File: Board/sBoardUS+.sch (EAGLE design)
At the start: 40 parts, among them IC1 PIC18F2580-E/SO, IC2 74AC32D, IC3 MAX481CSA, IC4 MC1525TT

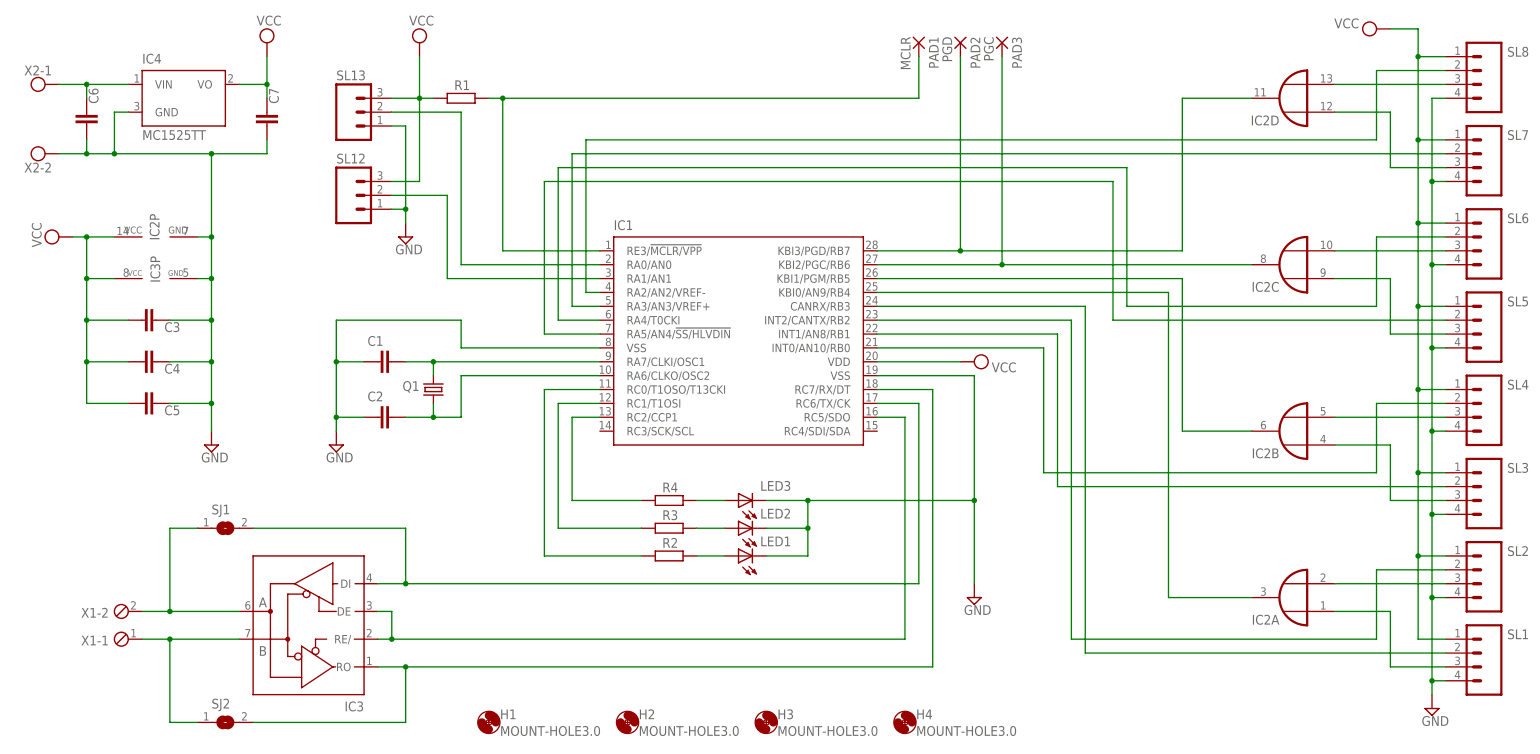
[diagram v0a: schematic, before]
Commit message: Aggiornamento struttura e modifiche
Cambiata la cartella di lavoro e ricreato il file BRD, modificato lo
schema aggiungendo il led di TX/RX, aggiunto il connettore I2C, cambiato
il quarzo.
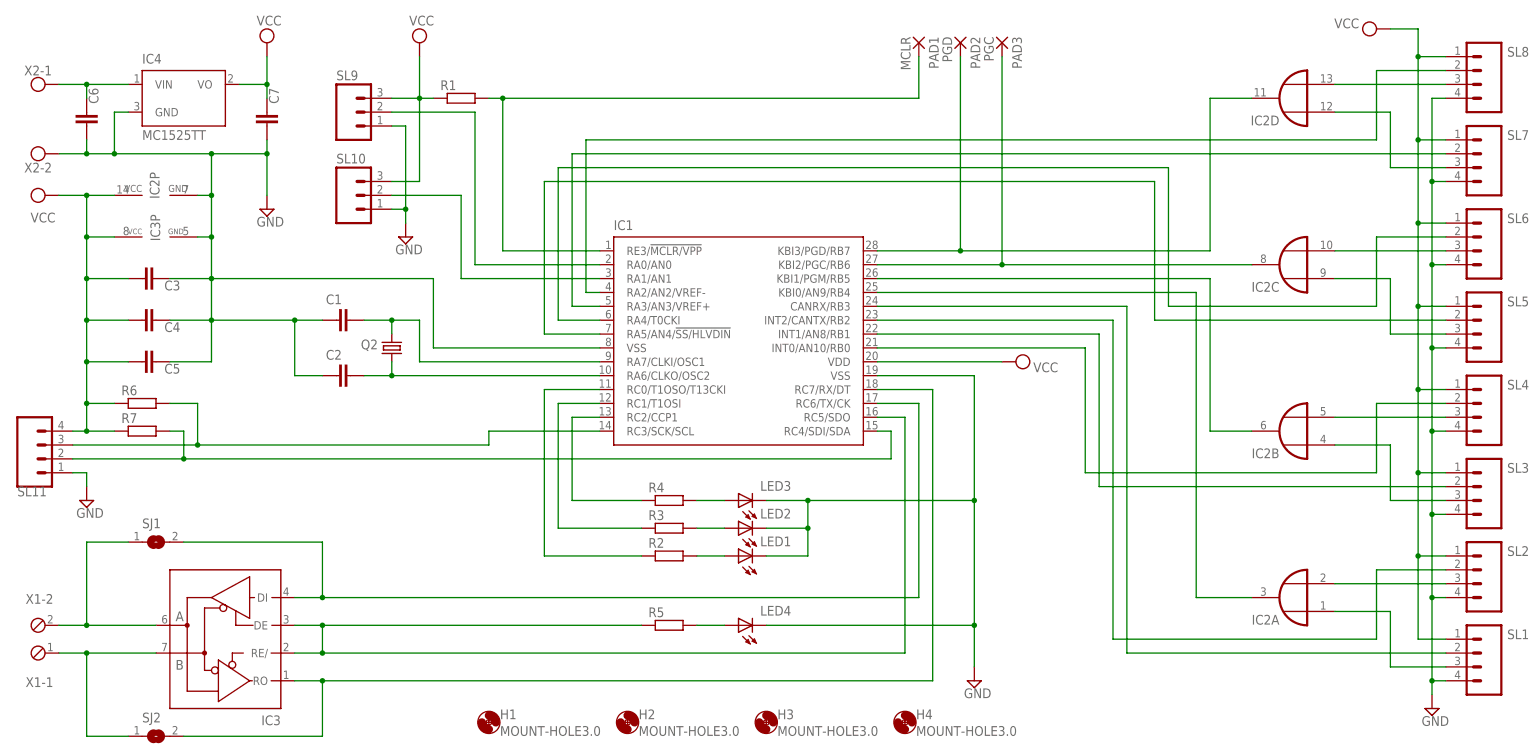
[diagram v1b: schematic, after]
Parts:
- removed Q1: (no value), crystal:CRYSTALHC49UP
- added LED4: (no value), led:LED
- added Q2: (no value), crystal:CRYSTALHC49U-V
- added R5, R6, R7: (no value), rcl:R-EU_R0805
- added SL11: (no value), con-amp-quick:M04
- R1, R2, R3, R4: device rcl:R-EU_M2012 -> rcl:R-EU_R0805
- renumbered SL12 to SL10, SL13 to SL9
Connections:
- new net N$38: LED4.A, R5.2
- new net N$39: IC1.RC3/SCK/SCL, R6.2, SL11.3
- new net N$40: IC1.RC4/SDI/SDA, R7.2, SL11.2
- net GND: now also LED4.C, SL11.1
- net N$1: now also Q2.2; no longer Q1.2
- net N$2: now also Q2.1; no longer Q1.1
- net N$27: now also R5.1
- net N$31: now also R2.1; no longer R2.2
- net N$32: now also R3.1; no longer R3.2
- net N$33: now also R4.1; no longer R4.2
- net N$34: now also R4.2; no longer R4.1
- net N$35: now also R3.2; no longer R3.1
- net N$36: now also R2.2; no longer R2.1
- net N$4: now also R1.2; no longer R1.1
- net VCC: now also R1.1, R6.1, R7.1, SL11.4; no longer R1.2
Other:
- moved on the sheet: C1, C2, C3, C4, C5, IC2P, IC3, IC3P, R1, R2, R3, R4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

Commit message: Invertite le porte OR per ridurre gli incroci delle piste
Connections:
- net N$10: now also IC2A.O; no longer IC2D.O
- net N$11: now also IC2B.I1, SL6.3; no longer IC2A.I1, SL2.3
- net N$12: now also IC2C.I1, SL4.3; no longer IC2D.I1, SL8.3
- net N$13: now also IC2D.I1, SL2.3; no longer IC2C.I1, SL6.3
- net N$14: now also IC2A.I0; no longer IC2D.I0
- net N$15: now also IC2B.I0; no longer IC2C.I0
- net N$16: now also IC2C.I0; no longer IC2B.I0
- net N$17: now also IC2D.I0; no longer IC2A.I0
- net N$3: now also IC2A.I1, SL8.3; no longer IC2B.I1, SL4.3
- net N$7: now also IC2D.O; no longer IC2A.O
- net N$8: now also IC2C.O; no longer IC2B.O
- net N$9: now also IC2B.O; no longer IC2C.O
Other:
- moved on the sheet: IC2A, IC2B, IC2C, IC2D
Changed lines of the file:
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@@
 <instance part="SL10" gate="G$1" x="15.24" y="73.66"/>
 <instance part="SL9" gate="G$1" x="15.24" y="88.9"/>
-<instance part="IC2" gate="A" x="187.96" y="0" rot="R180"/>
-<instance part="IC2" gate="B" x="187.96" y="30.48" rot="R180"/>
-<instance part="IC2" gate="C" x="187.96" y="60.96" rot="R180"/>
-<instance part="IC2" gate="D" x="187.96" y="91.44" rot="R180"/>
+<instance part="IC2" gate="A" x="187.96" y="91.44" rot="R180"/>
+<instance part="IC2" gate="B" x="187.96" y="60.96" rot="R180"/>
+<instance part="IC2" gate="C" x="187.96" y="30.48" rot="R180"/>
+<instance part="IC2" gate="D" x="187.96" y="0" rot="R180"/>
 <instance part="IC2" gate="P" x="-20.32" y="73.66" rot="R90"/>
 <instance part="SUPPLY3" gate="GND" x="25.4" y="66.04"/>
@@
 <net name="N$7" class="0">
 <segment>
-<pinref part="IC2" gate="A" pin="O"/>
-<wire x1="180.34" y1="0" x2="170.18" y2="0" width="0.1524" layer="91"/>
 <wire x1="170.18" y1="0" x2="170.18" y2="55.88" width="0.1524" layer="91"/>
 <pinref part="IC1" gate="G$1" pin="KBI0/AN9/RB4"/>
 <wire x1="170.18" y1="55.88" x2="111.76" y2="55.88" width="0.1524" layer="91"/>
+<pinref part="IC2" gate="D" pin="O"/>
+<wire x1="180.34" y1="0" x2="170.18" y2="0" width="0.1524" layer="91"/>
 </segment>
 </net>
@@
 <wire x1="111.76" y1="58.42" x2="172.72" y2="58.42" width="0.1524" layer="91"/>
 <wire x1="172.72" y1="58.42" x2="172.72" y2="30.48" width="0.1524" layer="91"/>
-<pinref part="IC2" gate="B" pin="O"/>
-<wire x1="172.72" y1="30.48" x2="180.34" y2="30.48" width="0.1524" layer="91"/>
+<pinref part="IC2" gate="C" pin="O"/>
+<wire x1="180.34" y1="30.48" x2="172.72" y2="30.48" width="0.1524" layer="91"/>
 </segment>
 </net>
 <net name="N$9" class="0">
 <segment>
-<pinref part="IC2" gate="C" pin="O"/>
 <pinref part="IC1" gate="G$1" pin="KBI2/PGC/RB6"/>
-<wire x1="180.34" y1="60.96" x2="134.62" y2="60.96" width="0.1524" layer="91"/>
 <wire x1="134.62" y1="60.96" x2="111.76" y2="60.96" width="0.1524" layer="91"/>
 <wire x1="134.62" y1="99.06" x2="134.62" y2="60.96" width="0.1524" layer="91"/>
+<pinref part="PAD3" gate="1" pin="P"/>
+<pinref part="IC2" gate="B" pin="O"/>
+<wire x1="180.34" y1="60.96" x2="134.62" y2="60.96" width="0.1524" layer="91"/>
 <junction x="134.62" y="60.96"/>
-<pinref part="PAD3" gate="1" pin="P"/>
 </segment>
 </net>
@@
 <wire x1="127" y1="63.5" x2="172.72" y2="63.5" width="0.1524" layer="91"/>
 <wire x1="172.72" y1="63.5" x2="172.72" y2="91.44" width="0.1524" layer="91"/>
-<pinref part="IC2" gate="D" pin="O"/>
-<wire x1="172.72" y1="91.44" x2="180.34" y2="91.44" width="0.1524" layer="91"/>
 <wire x1="127" y1="99.06" x2="127" y2="63.5" width="0.1524" layer="91"/>
 <junction x="127" y="63.5"/>
 <pinref part="PAD2" gate="1" pin="P"/>
-</segment>
-</net>
-<net name="N$12" class="0">
-<segment>
-<pinref part="SL8" gate="G$1" pin="3"/>
-<pinref part="IC2" gate="D" pin="I1"/>
-<wire x1="215.9" y1="93.98" x2="195.58" y2="93.98" width="0.1524" layer="91"/>
-</segment>
-</net>
-<net name="N$13" class="0">
-<segment>
-<pinref part="IC2" gate="C" pin="I1"/>
-<pinref part="SL6" gate="G$1" pin="3"/>
-<wire x1="195.58" y1="63.5" x2="215.9" y2="63.5" width="0.1524" layer="91"/>
-</segment>
-</net>
-<net name="N$3" class="0">
-<segment>
-<pinref part="IC2" gate="B" pin="I1"/>
-<pinref part="SL4" gate="G$1" pin="3"/>
-<wire x1="195.58" y1="33.02" x2="215.9" y2="33.02" width="0.1524" layer="91"/>
-</segment>
-</net>
-<net name="N$11" class="0">
-<segment>
-<pinref part="IC2" gate="A" pin="I1"/>
-<pinref part="SL2" gate="G$1" pin="3"/>
-<wire x1="195.58" y1="2.54" x2="215.9" y2="2.54" width="0.1524" layer="91"/>
+<pinref part="IC2" gate="A" pin="O"/>
+<wire x1="180.34" y1="91.44" x2="172.72" y2="91.44" width="0.1524" layer="91"/>
 </segment>
 </net>
@@
 <wire x1="215.9" y1="78.74" x2="205.74" y2="78.74" width="0.1524" layer="91"/>
 <wire x1="205.74" y1="78.74" x2="205.74" y2="88.9" width="0.1524" layer="91"/>
-<pinref part="IC2" gate="D" pin="I0"/>
-<wire x1="205.74" y1="88.9" x2="195.58" y2="88.9" width="0.1524" layer="91"/>
+<pinref part="IC2" gate="A" pin="I0"/>
+<wire x1="195.58" y1="88.9" x2="205.74" y2="88.9" width="0.1524" layer="91"/>
 </segment>
 </net>
@@
 <wire x1="215.9" y1="48.26" x2="205.74" y2="48.26" width="0.1524" layer="91"/>
 <wire x1="205.74" y1="48.26" x2="205.74" y2="58.42" width="0.1524" layer="91"/>
-<pinref part="IC2" gate="C" pin="I0"/>
+<pinref part="IC2" gate="B" pin="I0"/>
 <wire x1="205.74" y1="58.42" x2="195.58" y2="58.42" width="0.1524" layer="91"/>
 </segment>
@@
 <wire x1="215.9" y1="17.78" x2="205.74" y2="17.78" width="0.1524" layer="91"/>
 <wire x1="205.74" y1="17.78" x2="205.74" y2="27.94" width="0.1524" layer="91"/>
-<pinref part="IC2" gate="B" pin="I0"/>
-<wire x1="205.74" y1="27.94" x2="195.58" y2="27.94" width="0.1524" layer="91"/>
+<pinref part="IC2" gate="C" pin="I0"/>
+<wire x1="195.58" y1="27.94" x2="205.74" y2="27.94" width="0.1524" layer="91"/>
 </segment>
 </net>
@@
 <wire x1="215.9" y1="-12.7" x2="205.74" y2="-12.7" width="0.1524" layer="91"/>
 <wire x1="205.74" y1="-12.7" x2="205.74" y2="-2.54" width="0.1524" layer="91"/>
-<pinref part="IC2" gate="A" pin="I0"/>
+<pinref part="IC2" gate="D" pin="I0"/>
 <wire x1="205.74" y1="-2.54" x2="195.58" y2="-2.54" width="0.1524" layer="91"/>
 </segment>
@@
 </segment>
 </net>
+<net name="N$3" class="0">
+<segment>
+<pinref part="IC2" gate="A" pin="I1"/>
+<pinref part="SL8" gate="G$1" pin="3"/>
+<wire x1="195.58" y1="93.98" x2="215.9" y2="93.98" width="0.1524" layer="91"/>
+</segment>
+</net>
+<net name="N$11" class="0">
+<segment>
+<pinref part="SL6" gate="G$1" pin="3"/>
+<pinref part="IC2" gate="B" pin="I1"/>
+<wire x1="215.9" y1="63.5" x2="195.58" y2="63.5" width="0.1524" layer="91"/>
+</segment>
+</net>
+<net name="N$12" class="0">
+<segment>
+<pinref part="SL4" gate="G$1" pin="3"/>
+<pinref part="IC2" gate="C" pin="I1"/>
+<wire x1="215.9" y1="33.02" x2="195.58" y2="33.02" width="0.1524" layer="91"/>
+</segment>
+</net>
+<net name="N$13" class="0">
+<segment>
+<pinref part="SL2" gate="G$1" pin="3"/>
+<pinref part="IC2" gate="D" pin="I1"/>
+<wire x1="215.9" y1="2.54" x2="195.58" y2="2.54" width="0.1524" layer="91"/>
+</segment>
+</net>
